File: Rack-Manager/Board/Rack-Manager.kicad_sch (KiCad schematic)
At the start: 0 parts

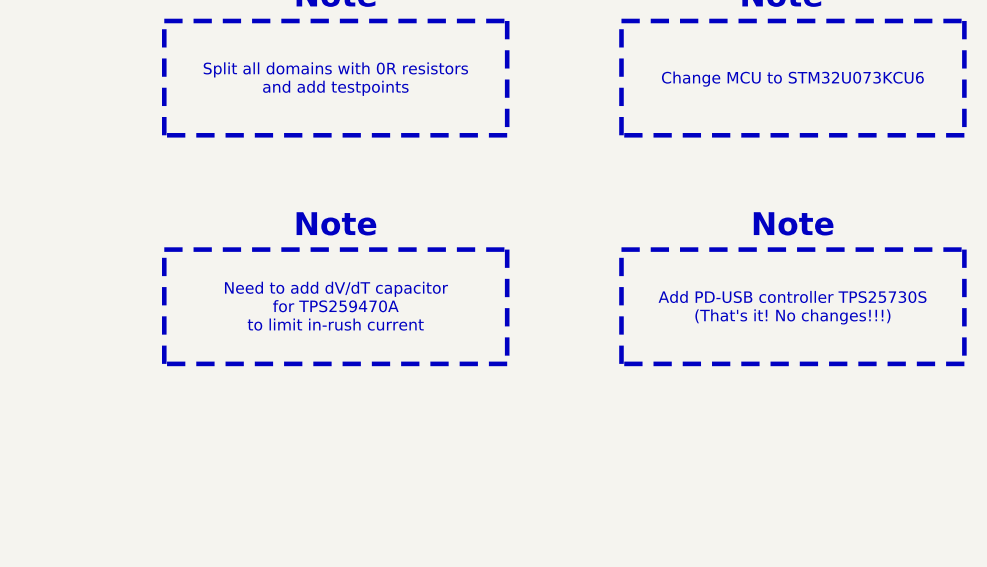
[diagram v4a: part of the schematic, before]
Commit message: Added dvdt cap on eFuses and choose PD standalone sink controller
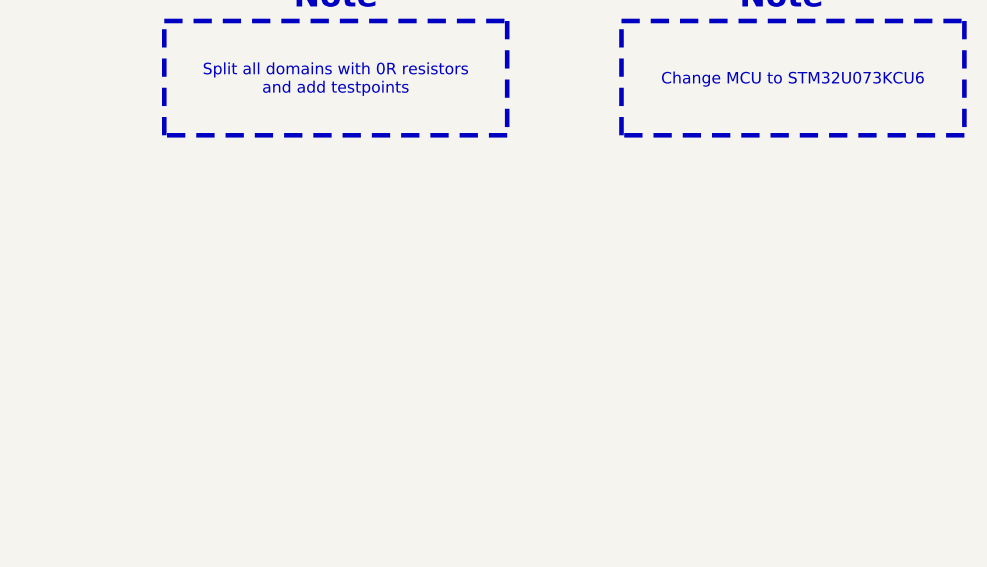
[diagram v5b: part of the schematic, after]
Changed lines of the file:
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@@
-	(text "Note"
-		(exclude_from_sim no)
-		(at 387.35 73.66 0)
-		(effects
-			(font
-				(size 2.54 2.54)
-				(thickness 0.508)
-				(bold yes)
-				(color 194 0 0 1)
-			)
-		)
-	)
 	(text "Note"
 		(exclude_from_sim no)
@@
 	(text "Note"
 		(exclude_from_sim no)
-		(at 336.55 73.66 0)
-		(effects
-			(font
-				(size 2.54 2.54)
-				(thickness 0.508)
-				(bold yes)
-				(color 194 0 0 1)
-			)
-		)
-	)
-	(text "Note"
-		(exclude_from_sim no)
 		(at 386.08 48.26 0)
 		(effects
@@
 				(bold yes)
 				(color 194 0 0 1)
-			)
-		)
-	)
-	(text_box "Need to add dV/dT capacitor\nfor TPS259470A\nto limit in-rush current"
-		(exclude_from_sim no)
-		(at 317.5 76.2 0)
-		(size 38.1 12.7)
-		(margins 0.9525 0.9525 0.9525 0.9525)
-		(stroke
-			(width 0.508)
-			(type dot)
-			(color 194 0 0 1)
-		)
-		(fill
-			(type color)
-			(color 255 165 169 1)
-		)
-		(effects
-			(font
-				(size 1.27 1.27)
 			)
 		)
@@
 		(size 38.1 12.7)
 		(margins 0.9525 0.9525 0.9525 0.9525)
-		(stroke
-			(width 0.508)
-			(type dot)
-			(color 194 0 0 1)
-		)
-		(fill
-			(type color)
-			(color 255 165 169 1)
-		)
-		(effects
-			(font
-				(size 1.27 1.27)
-			)
-		)
-	)
-	(text_box "Add PD-USB controller TPS25730S\n(That's it! No changes!!!)"
-		(exclude_from_sim no)
-		(at 368.3 76.2 0)
-		(size 38.1 12.7)
-		(margins 0.9525 0.9525 0.9525 0.9525)

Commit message: Added/Updated notes for TODOs
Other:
- note added: "Debug/Programming stuff"
- note added: "EMI ESD protection and logic"
- note added: "Footprints or parts missing"
